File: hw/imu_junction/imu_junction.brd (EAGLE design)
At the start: 62 x 24 mm, 50 parts, among them J1 JST-PH3SMT_VERT, J2 JST-PH3SMT_VERT, J3 JST-PH3SMT_VERT, J4 JST-PH3SMT_VERT, J5 JST-XH4SMT_RA, U1 STM32F4R_64PIN, U2 BMI088LGA16, U3 TPS62177WSON10, U4 SN65HVD75SOIC8, U5 SN65HVD75SOIC8, U6 SN65HVD75SOIC8, X1 8.0MHz

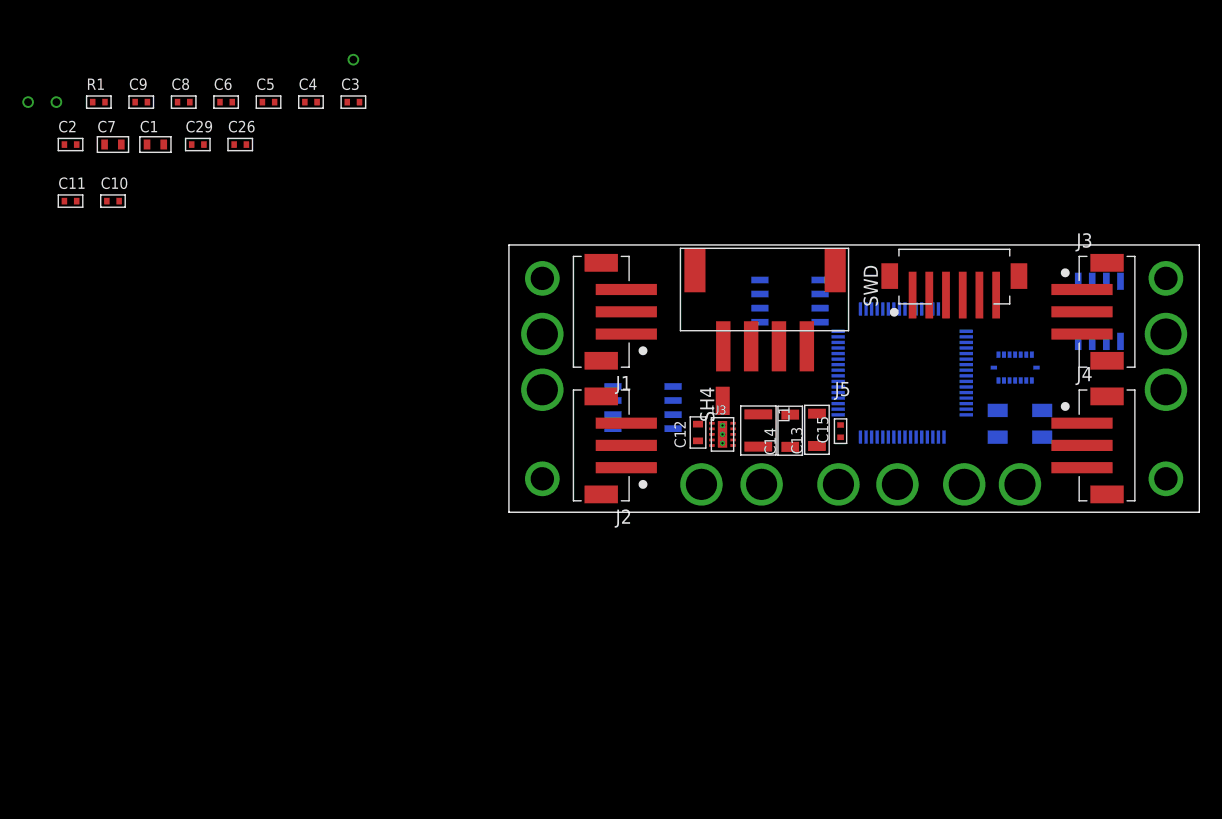
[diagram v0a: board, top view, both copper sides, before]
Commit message: More work on IMU junction board
Everything roughly placed on the board
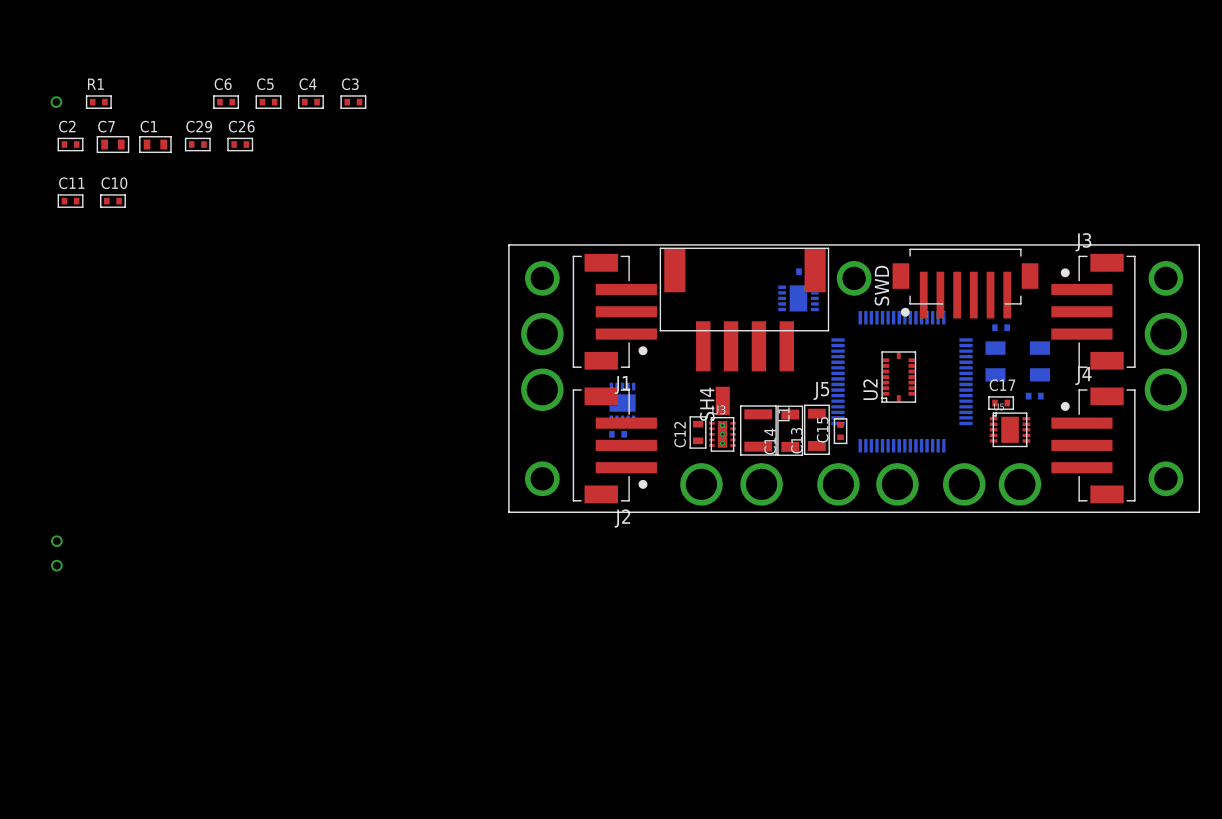
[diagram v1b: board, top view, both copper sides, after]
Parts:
- added C16, C17, C18: 0.1uF 50V, mfpassives:C0402
- added U$5: MOUNTM2, controller:M2MOUNT
- U4, U5, U6: value SN65HVD75SOIC8 -> MAX13431E; device imu_junction:SOIC8 -> controller:TDFN10
- moved C9 84.5 mm to (47.2, 10.4), flipped to the bottom
- moved C8 76.1 mm to (44.2, 16.6), flipped to the bottom, turned to 180 degrees
- moved DTX 52.7 mm to (-40.6, -4.80)
- moved DRX 39.5 mm to (-40.6, -2.60)
- moved U5 13.3 mm to (45.0, 7.40), flipped to the top, turned to 0 degrees
- moved U2 10.5 mm to (35.0, 12.1), flipped to the top, turned to 90 degrees
- moved X1 5.60 mm to (45.7, 13.5)
- moved U4 1.88 mm to (10.2, 9.80), turned to 270 degrees
- moved J5 1.80 mm to (21.2, 19.5)
- moved SWD 1.00 mm to (41.0, 21.5)
- moved U6 0.80 mm to (26.0, 19.2)
- moved U1 0.78 mm to (35.3, 11.7), turned to 0 degrees
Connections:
- new net DIR1: U1.39, U4.3, U4.4
- new net DIR2: U1.15, U5.3, U5.4
- new net DIR3: U1.53, U6.3, U6.4
- new net IMU_CS1: U1.58, U2.14
- new net IMU_CS2: U1.59, U2.5
- new net IMU_MISO: U1.56, U2.10, U2.15
- new net IMU_MOSI: U1.57, U2.9
- new net IMU_SCK: U1.55, U2.8
- new net RX1: U1.38, U4.2
- new net RX2: U1.17, U5.2
- new net RX3: U1.52, U6.2
- new net TX1: U1.37, U4.5
- new net TX2: U1.16, U5.5
- new net TX3: U1.51, U6.5
- net +3V3: now also C16.P$1, C17.P$1, C18.P$1, U4.1, U4.10, U5.1, U5.10, U6.1, U6.10
- net GND: now also C16.P$2, C17.P$2, C18.P$2, U4.6, U4.PAD, U5.6, U5.PAD, U6.6, U6.PAD; no longer U4.5, U5.5, U6.5
- net N$2: now also U1.42; no longer U1.58
- net N$3: now also U1.43; no longer U1.59
- net N$4: now also U5.8; no longer U5.6
- net N$5: now also U5.9; no longer U5.7
- net N$8: now also U4.9; no longer U4.7
- net N$9: no longer U4.6
- net SLAVE_RX: now also U6.8; no longer U6.6
- net SLAVE_TX: now also U6.9; no longer U6.7

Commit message: Progress on imu-junction
Parts placed and power routed
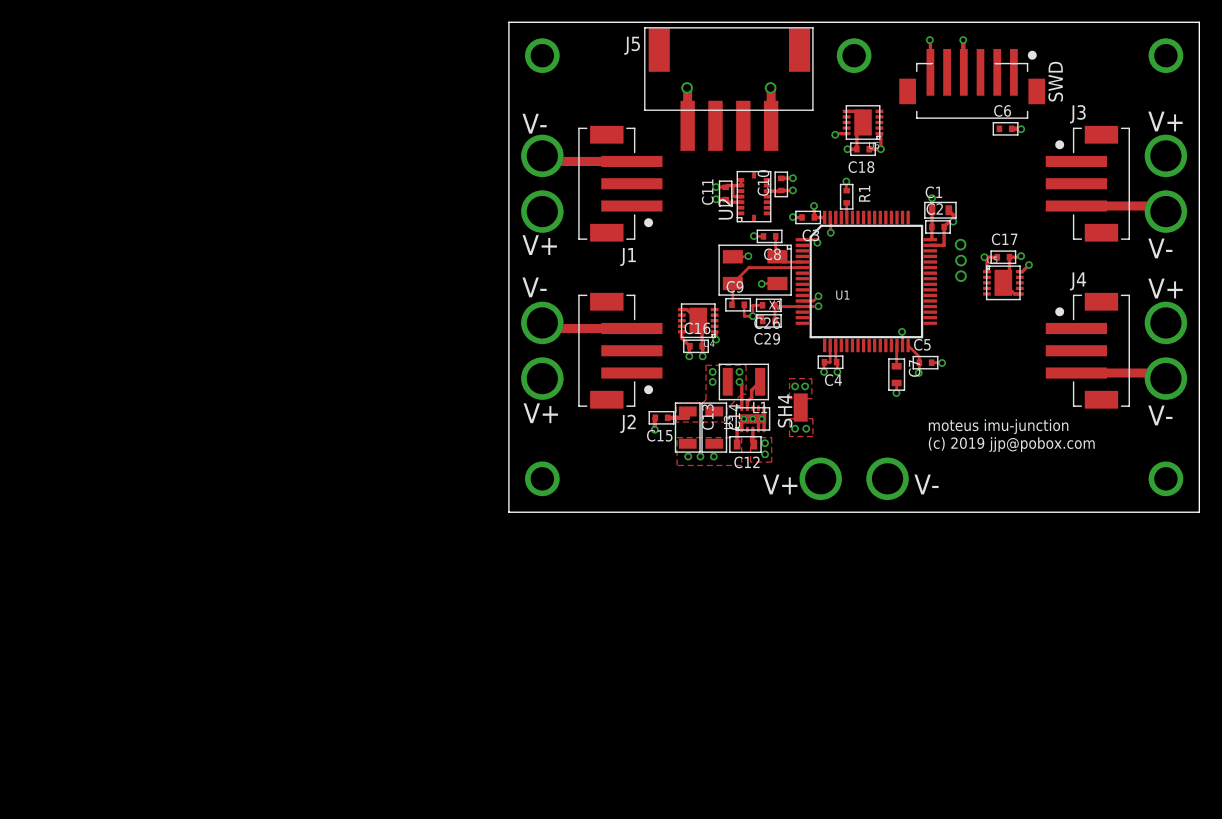
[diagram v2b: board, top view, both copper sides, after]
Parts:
- moved DTX 85.3 mm to (40.6, 21.2)
- moved DRX 85.0 mm to (40.6, 22.6)
- moved DGND 82.2 mm to (40.6, 24.0)
- moved C2 78.3 mm to (38.5, 25.6)
- moved C7 73.3 mm to (34.8, 12.4), turned to 270 degrees
- moved C1 70.7 mm to (38.8, 27.1)
- moved C6 70.0 mm to (44.6, 34.4)
- moved R1 67.7 mm to (30.3, 28.3), turned to 270 degrees
- moved C5 63.5 mm to (37.4, 13.4)
- moved C10 60.0 mm to (24.5, 29.4), turned to 90 degrees
- moved C11 58.8 mm to (19.5, 28.6), turned to 90 degrees
- moved C29 53.7 mm to (23.3, 17.2), turned to 180 degrees
- moved C4 52.2 mm to (28.9, 13.5), turned to 180 degrees
- moved C26 49.6 mm to (23.3, 18.6), turned to 180 degrees
- moved C3 42.1 mm to (26.9, 26.5), turned to 180 degrees
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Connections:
- new net IMU_ACC_INT: U1.3, U2.16
- new net IMU_GYRO_INT: U1.2, U2.12
- net DIR1: now also U1.15; no longer U1.39
- net DIR2: now also U1.39; no longer U1.15
- net GND: now also U2.7; no longer C13.P$2, C14.P$2, C15.P$2, J1.3, J2.3, J3.3, J4.3, J5.1, U3.5
- net N$9: now also U4.8
- net RX1: now also U1.17; no longer U1.38
- net RX2: now also U1.38; no longer U1.17
- net TX1: now also U1.16; no longer U1.37
- net TX2: now also U1.37; no longer U1.16
- net V-: now also C13.P$2, C14.P$2, C15.P$2, J1.3, J2.3, J3.3, J4.3, J5.1, U3.4, U3.5
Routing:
- net GND: track 0.00 -> 50.8 mm, vias 0 -> 22
- net V-: track 0.00 -> 43.7 mm, vias 0 -> 7
- net +3V3: track 0.00 -> 41.3 mm, vias 0 -> 19
- net N$36: track 0.00 -> 8.78 mm
- net +18V: track 0.00 -> 4.80 mm, vias 0 -> 3
- net N$35: track 0.00 -> 4.33 mm
- net N$1: track 0.00 -> 2.85 mm
- net N$23: track 0.00 -> 1.87 mm
- net N$33: track 0.00 -> 1.33 mm
- added copper zone on layer 1, net +18V
- added copper zone on layer 15, net +18V
- added copper zone on layer 1, net +3V3
- added copper zone on layer 15, net +3V3
- added copper zone on layer 1, net GND
- added copper zone on layer 2, net GND
- added copper zone on layer 1, net V-
- added copper zone on layer 2, net V-
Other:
- board size 62 x 24 mm -> 62 x 44 mm
- board text added: "(c) 2019 jjp@pobox.com"
- board text added: "V+"
- board text added: "V-"
- board text added: "moteus imu-junction"

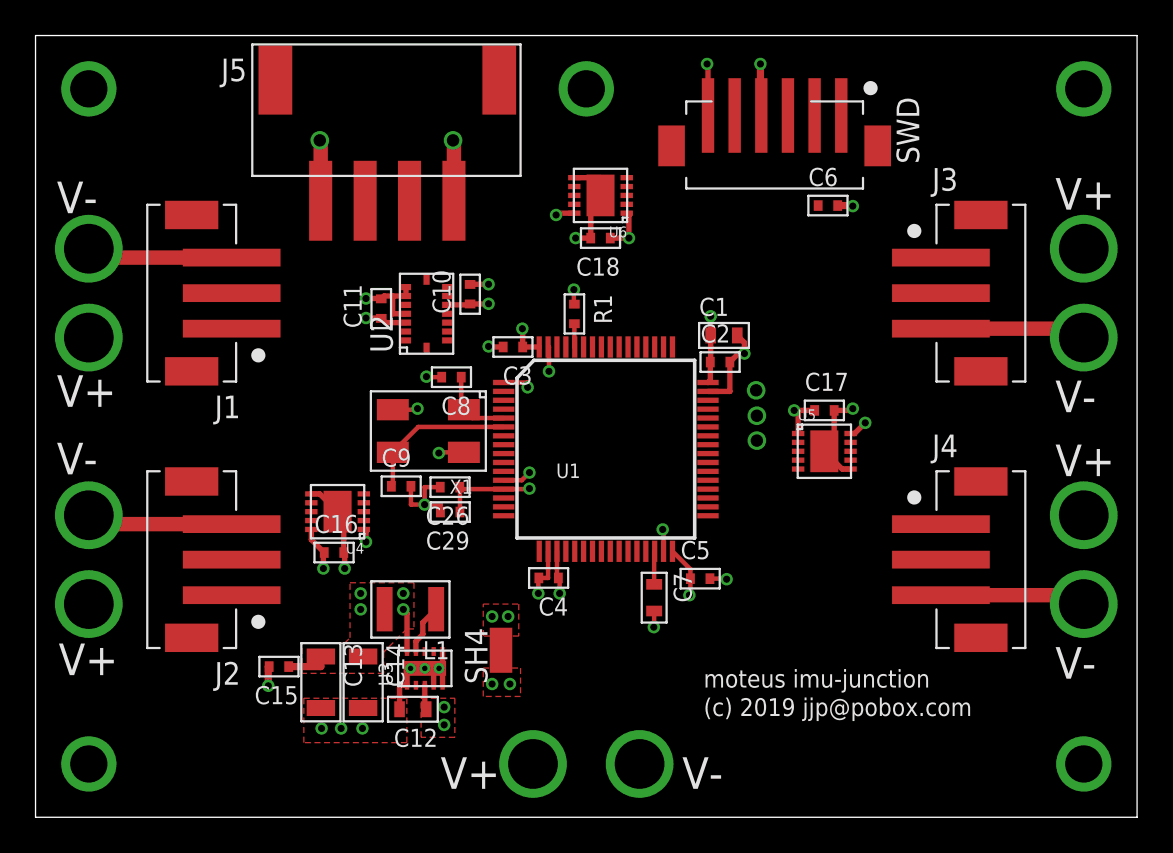
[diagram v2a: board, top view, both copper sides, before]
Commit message: imu_junction: Align all parts and rough align silk
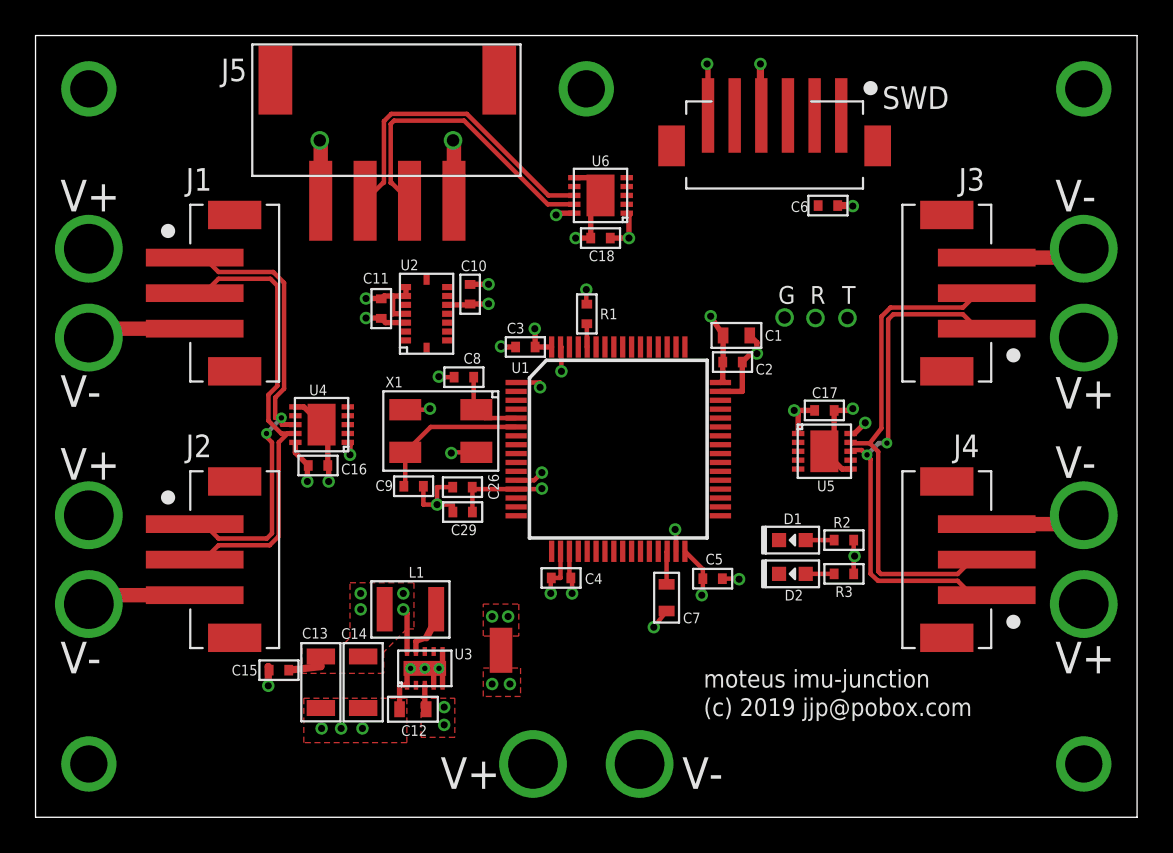
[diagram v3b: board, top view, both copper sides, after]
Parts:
- added D1: MF-LED-0603-RED, mfleds:LED0603
- added D2: MF-LED-0603-GREEN, mfleds:LED0603
- added R2, R3: 220, mfpassives:R0402
- moved DTX 8.58 mm to (45.7, 28.1)
- moved DRX 6.41 mm to (43.9, 28.1)
- moved V+1 5.00 mm to (3.00, 32.0)
- moved V+2 5.00 mm to (3.00, 17.0)
- moved V+3 5.00 mm to (59.0, 27.0)
- moved V+4 5.00 mm to (59.0, 12.0)
- moved V-1 5.00 mm to (3.00, 27.0)
- moved V-2 5.00 mm to (3.00, 12.0)
- moved V-3 5.00 mm to (59.0, 32.0)
- moved V-4 5.00 mm to (59.0, 17.0)
- moved U4 4.98 mm to (16.1, 22.1)
- moved C16 4.98 mm to (15.9, 19.8)
- moved DGND 4.40 mm to (42.2, 28.1)
- moved J1 3.00 mm to (11.5, 29.5), turned to 270 degrees
- moved J2 3.00 mm to (11.5, 14.5), turned to 270 degrees
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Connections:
- net N$4 renamed D2_P
- net N$5 renamed D2_N
- net N$8 renamed D1_N
- net N$9 renamed D1_P
- net SLAVE_RX renamed D3_P
- net SLAVE_TX renamed D3_N
- new net N$5: D1.ANODE, R2.P$1
- new net N$8: D2.ANODE, R3.P$1
- new net STATUS1: D1.CATHODE, U1.34
- new net STATUS2: D2.CATHODE, U1.33
- net +3V3: now also R2.P$2, R3.P$2
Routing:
- net D2_P: track 0.00 -> 29.6 mm, vias 0 -> 2
- net D2_N: track 0.00 -> 28.8 mm
- net D1_P: track 0.00 -> 27.8 mm, vias 0 -> 2
- net D1_N: track 0.00 -> 26.5 mm
- net D3_P: track 0.00 -> 17.7 mm
- net D3_N: track 0.00 -> 17.2 mm
- net V-: track 43.7 -> 34.5 mm
- net +3V3: track 41.3 -> 43.4 mm, vias 19 -> 20
- net N$8: track 0.00 -> 1.60 mm
- net N$5: track 0.00 -> 1.60 mm
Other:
- board text added: "G"
- board text added: "R"
- board text added: "T"

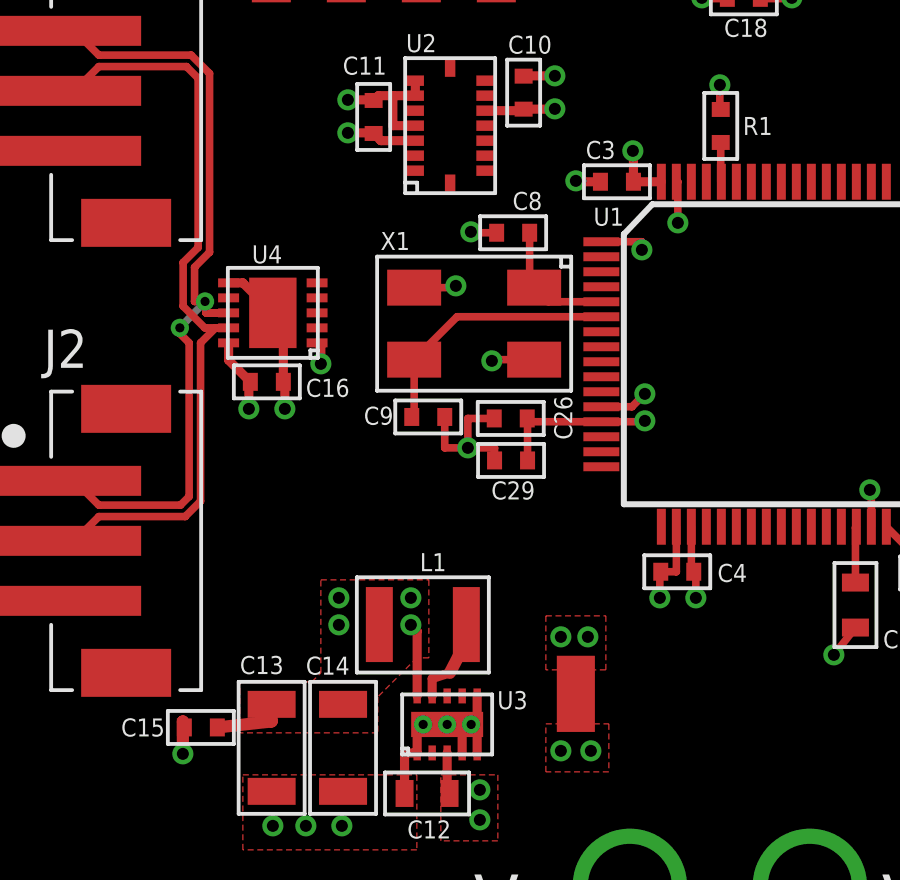
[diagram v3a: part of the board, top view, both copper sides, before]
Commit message: imu_junction: Finalize BOM
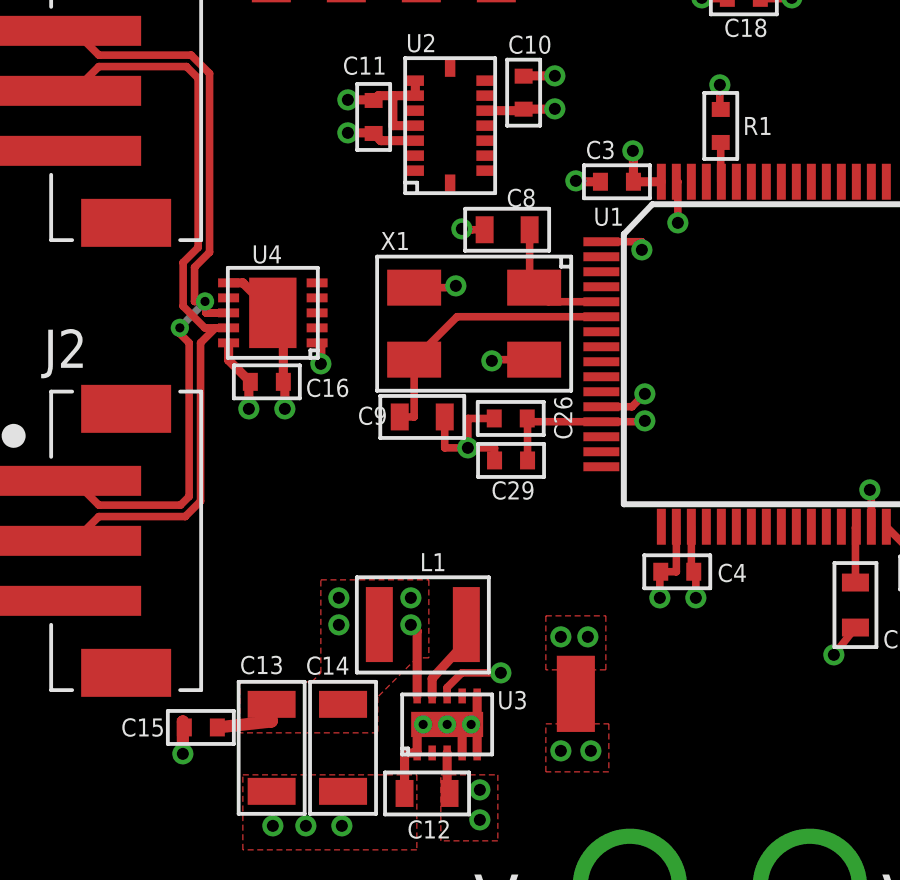
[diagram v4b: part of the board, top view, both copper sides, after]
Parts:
- C29: value 1uF 35V -> 1uF
- C8, C9: device mfpassives:C0402 -> mfpassives:C0603
- moved C8 0.22 mm to (23.9, 24.9)
- moved C9 0.20 mm to (21.1, 18.6)
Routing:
- net +3V3: track 43.4 -> 45.7 mm, vias 20 -> 21
